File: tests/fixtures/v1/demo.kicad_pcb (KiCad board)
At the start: 2 copper layers, 30 x 20 mm, 2 parts

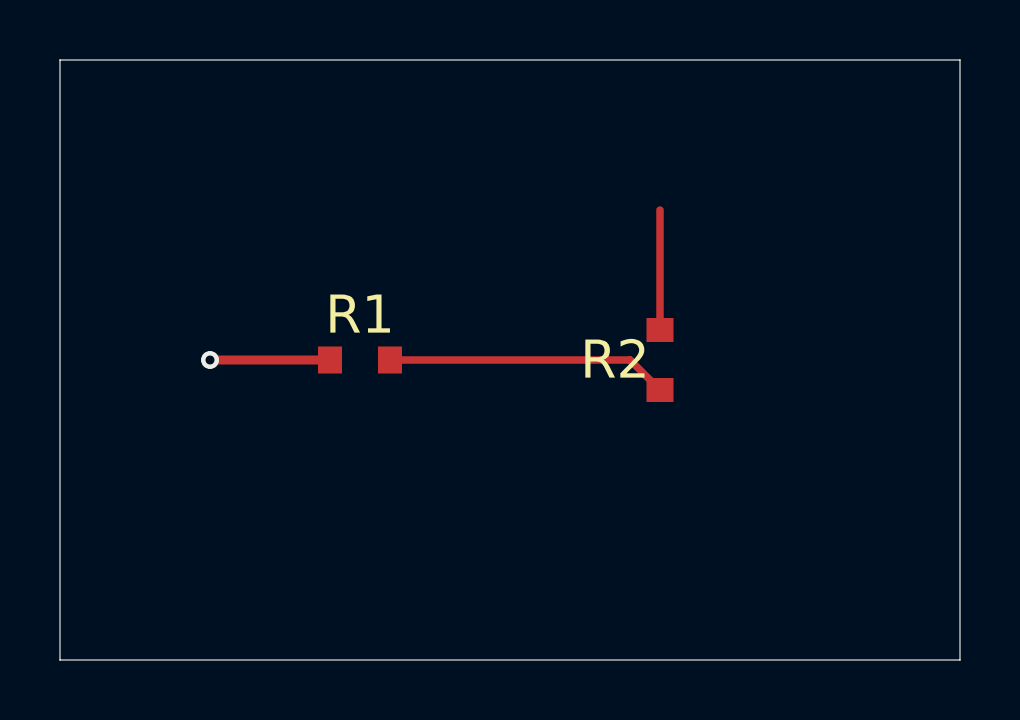
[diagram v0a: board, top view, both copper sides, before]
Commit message: [chore] Detected board change also now covers footprint changes
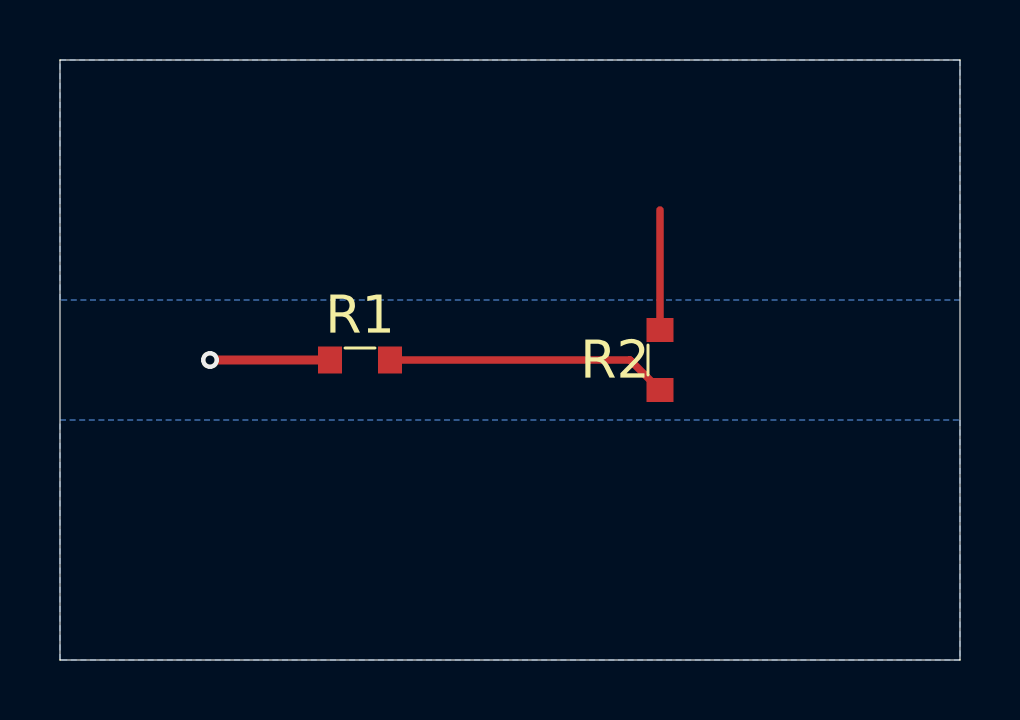
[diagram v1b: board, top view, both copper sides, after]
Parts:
- R1, R2: value (none) -> 1k
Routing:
- added copper zone on B.Cu, net GND
- added copper zone on B.Cu, net VCC
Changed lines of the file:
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@@
 			(layer "F.SilkS")
+		)
+		(property "Value" "1k"
+			(at 0 1.5 0)
+			(layer "F.Fab")
+		)
+		(fp_line
+			(start -0.5 -0.4)
+			(end 0.5 -0.4)
+			(stroke (width 0.1) (type solid))
+			(layer "F.SilkS")
+			(uuid "fp-r1-silk")
 		)
 		(pad "1" smd rect
@@
 			(at 0 -1.5 0)
 			(layer "F.SilkS")
+		)
+		(property "Value" "1k"
+			(at 0 1.5 0)
+			(layer "F.Fab")
+		)
+		(fp_line
+			(start -0.5 -0.4)
+			(end 0.5 -0.4)
+			(stroke (width 0.1) (type solid))
+			(layer "F.SilkS")
+			(uuid "fp-r2-silk")
 		)
 		(pad "1" smd rect
@@
 		(uuid "via-1")
 	)
+	(zone
+		(net "GND")
+		(layer "B.Cu")
+		(uuid "zone-gnd")
+		(hatch edge 0.5)
+		(connect_pads (clearance 0.5))
+		(min_thickness 0.25)
+		(fill yes (thermal_gap 0.5) (thermal_bridge_width 0.5))
+		(polygon (pts (xy 0 0) (xy 30 0) (xy 30 8) (xy 0 8)))
+	)
+	(zone
+		(net "VCC")
+		(layer "B.Cu")
+		(uuid "zone-vcc")
+		(hatch edge 0.5)
+		(connect_pads (clearance 0.5))
+		(min_thickness 0.25)
+		(fill yes (thermal_gap 0.5) (thermal_bridge_width 0.5))
+		(polygon (pts (xy 0 12) (xy 30 12) (xy 30 20) (xy 0 20)))
+	)
 )
